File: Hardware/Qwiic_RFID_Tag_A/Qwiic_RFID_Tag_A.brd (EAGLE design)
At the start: 25.4 x 50.8 mm, 46 parts, among them J1 Qwiic, J2 Qwiic, U1 ST25DV64KC

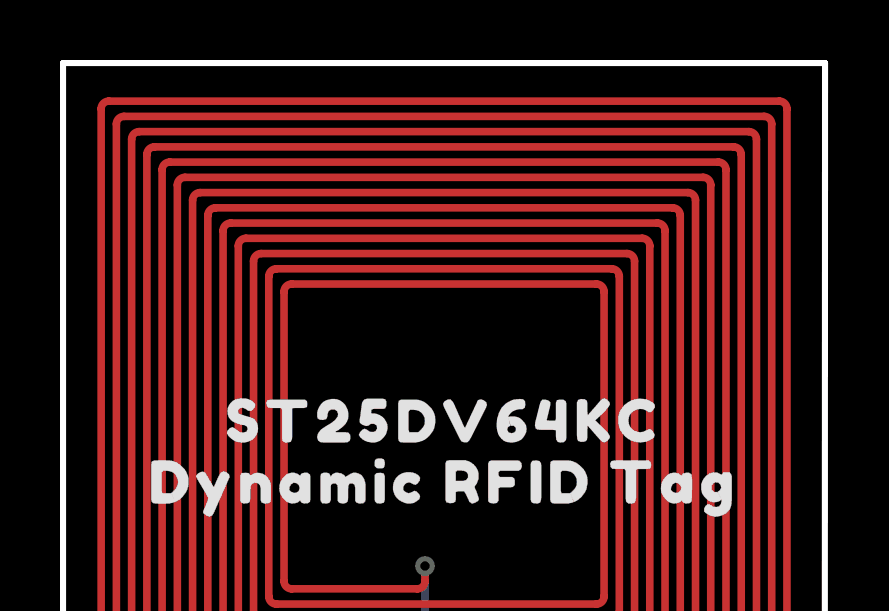
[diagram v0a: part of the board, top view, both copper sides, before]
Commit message: Update aesthetics
Add SFE logo
Update version number
Change schematic frame to correct version
Update design attribution
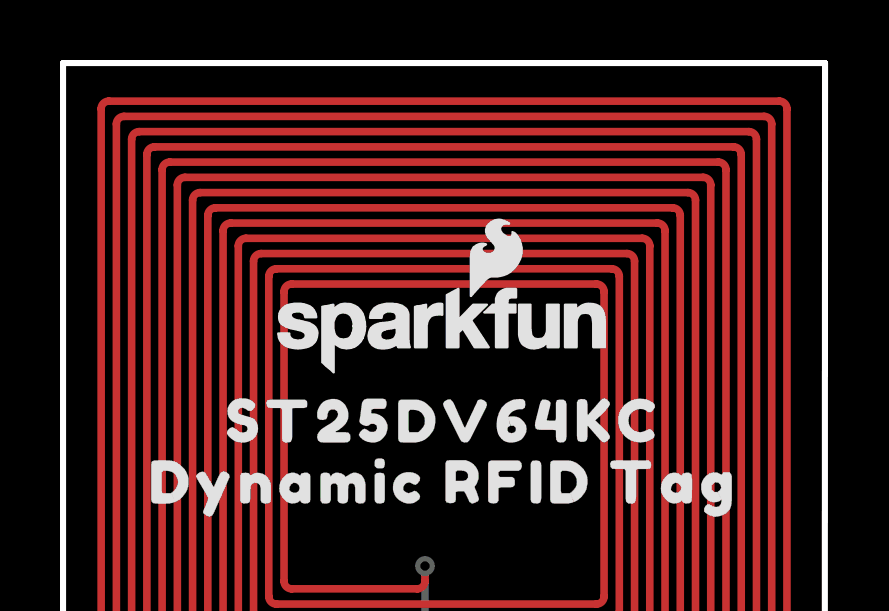
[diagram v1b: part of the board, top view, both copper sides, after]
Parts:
- removed FRAME1: FRAME-LETTERNO_PACKAGE, SparkFun-Aesthetics:DUMMY
- added FRAME2: FRAME-LETTER, SparkFun-Aesthetics:CREATIVE_COMMONS
- added LOGO2, LOGO4: SFE_LOGO_NAME_FLAME.1_INCH, SparkFun-Aesthetics:SFE_LOGO_NAME_FLAME_.1
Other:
- board text added: "Revised by: Dryw Wade"
- board text added: "Ricardo Ramos"
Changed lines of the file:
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@@
 <drawing>
 <settings>
-<setting alwaysvectorfont="no"/>
+<setting alwaysvectorfont="yes"/>
 <setting verticaltext="up"/>
 </settings>
@@
 <layer number="38" name="bTest" color="7" fill="1" visible="no" active="yes"/>
 <layer number="39" name="tKeepout" color="4" fill="11" visible="yes" active="yes"/>
-<layer number="40" name="bKeepout" color="1" fill="11" visible="yes" active="yes"/>
+<layer number="40" name="bKeepout" color="1" fill="11" visible="no" active="yes"/>
 <layer number="41" name="tRestrict" color="4" fill="10" visible="yes" active="yes"/>
-<layer number="42" name="bRestrict" color="1" fill="10" visible="yes" active="yes"/>
-<layer number="43" name="vRestrict" color="2" fill="10" visible="yes" active="yes"/>
+<layer number="42" name="bRestrict" color="1" fill="10" visible="no" active="yes"/>
+<layer number="43" name="vRestrict" color="2" fill="10" visible="no" active="yes"/>
 <layer number="44" name="Drills" color="7" fill="1" visible="no" active="yes"/>
 <layer number="45" name="Holes" color="7" fill="1" visible="yes" active="yes"/>
-<layer number="46" name="Milling" color="3" fill="1" visible="yes" active="yes"/>
+<layer number="46" name="Milling" color="3" fill="1" visible="no" active="yes"/>
 <layer number="47" name="Measures" color="7" fill="1" visible="yes" active="yes"/>
 <layer number="48" name="Document" color="7" fill="1" visible="no" active="yes"/>
@@
 <layer number="50" name="dxf" color="7" fill="1" visible="no" active="no"/>
 <layer number="51" name="tDocu" color="6" fill="1" visible="yes" active="yes"/>
-<layer number="52" name="bDocu" color="7" fill="1" visible="yes" active="yes"/>
+<layer number="52" name="bDocu" color="7" fill="1" visible="no" active="yes"/>
 <layer number="53" name="tGND_GNDA" color="7" fill="9" visible="no" active="no"/>
 <layer number="54" name="bGND_GNDA" color="1" fill="9" visible="no" active="no"/>
@@
 <dimension x1="0" y1="0" x2="0" y2="22.86" x3="-8.89" y3="11.43" textsize="1.778" textratio="15" layer="47" unit="inch"/>
 <dimension x1="0" y1="0" x2="0" y2="50.8" x3="-12.7" y3="25.4" textsize="1.778" textratio="15" layer="47" unit="inch"/>
+<text x="16.51" y="-29.21" size="1.778" layer="51" font="vector">Ricardo Ramos</text>
+<text x="2.54" y="-31.75" size="1.778" layer="51" font="vector">Revised by: Dryw Wade</text>
 </plain>
 <attributes>
@@
 <attribute name="VALUE" x="22.86" y="19.685" size="0.6096" layer="27" font="vector" ratio="20" rot="R180" align="top-center"/>
 </element>
-<element name="FRAME1" library="SparkFun-Aesthetics" package="DUMMY" value="FRAME-LETTERNO_PACKAGE" x="0" y="0" smashed="yes">
-<attribute name="DESIGNER" value="Ricardo Ramos" x="33.02" y="-38.1" size="1.778" layer="27" display="off"/>
-<attribute name="REV" value="X02" x="0" y="0" size="1.778" layer="27" display="off"/>
-<attribute name="VERSION" value="x01" x="33.02" y="-38.1" size="1.778" layer="27" display="off"/>
-</element>
 <element name="J1" library="SparkFun-Connectors" package="JST04_1MM_RA" value="Qwiic" x="20.32" y="12.7" smashed="yes" rot="R90">
 <attribute name="NAME" x="22.479" y="11.303" size="0.6096" layer="25" font="vector" ratio="20" rot="R90"/>
@@
 <element name="U$11" library="output" package="DYNAMIC_RFID_TAG0" value="" x="12.7" y="36.83" smashed="yes" rot="MR0"/>
 <element name="U$1" library="output" package="#I2C#0" value="" x="9.525" y="12.7" smashed="yes" rot="MR0"/>
+<element name="FRAME2" library="SparkFun-Aesthetics" package="CREATIVE_COMMONS" value="FRAME-LETTER" x="-10.16" y="-29.21" smashed="yes">
+<attribute name="DESIGNER" value="" x="-10.16" y="-29.21" size="1.778" layer="27" display="off"/>
+<attribute name="REV" value="" x="-10.16" y="-29.21" size="1.778" layer="27" display="off"/>
+</element>
+<element name="LOGO2" library="SparkFun-Aesthetics" package="SFE_LOGO_NAME_FLAME_.1" value="SFE_LOGO_NAME_FLAME.1_INCH" x="12.7" y="41.91" smashed="yes"/>
+<element name="LOGO4" library="SparkFun-Aesthetics" package="SFE_LOGO_NAME_FLAME_.1" value="SFE_LOGO_NAME_FLAME.1_INCH" x="12.7" y="41.91" smashed="yes" rot="MR0"/>
 </elements>
 <signals>

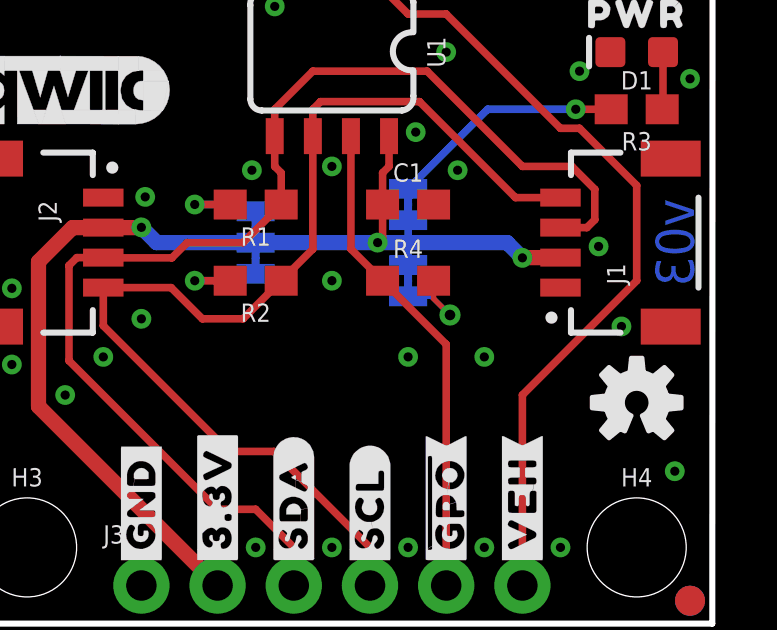
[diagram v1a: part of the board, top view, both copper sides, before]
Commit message: Design review updates
All scehmatics:
Change IC text to “Dynamic RFID Tag - ST25DV64KC”
Move decoupling capacitor near IC
Update I2C jumper text to say "traces" instead of "trace"

Version A board:
Fix stray via diameter
Approve jumper overlap error

Version C board:
Add SFE logo to bottom silk
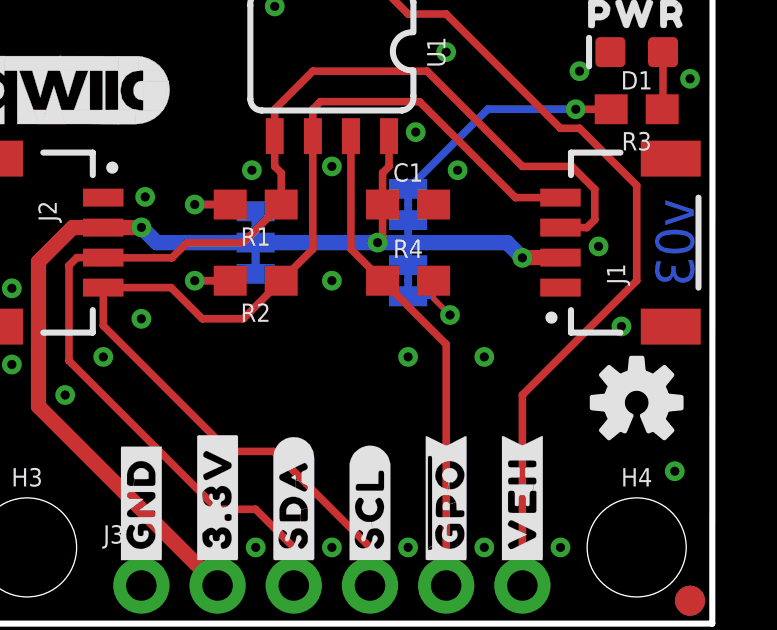
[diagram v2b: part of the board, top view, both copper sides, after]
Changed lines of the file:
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@@
 <drawing>
 <settings>
-<setting alwaysvectorfont="yes"/>
+<setting alwaysvectorfont="no"/>
 <setting verticaltext="up"/>
 </settings>
@@
 <wire x1="16.09" y1="11.43" x2="16.09" y2="10.834" width="0.1778" layer="1"/>
 <wire x1="16.09" y1="10.834" x2="16.637" y2="10.287" width="0.1778" layer="1"/>
-<via x="16.637" y="10.287" extent="1-16" drill="0.35"/>
+<via x="16.637" y="10.287" extent="1-16" drill="0.3048"/>
 <wire x1="16.637" y1="10.287" x2="16.0147" y2="10.9093" width="0.1778" layer="16"/>
 <wire x1="16.0147" y1="10.9093" x2="15.24" y2="10.9093" width="0.1778" layer="16"/>

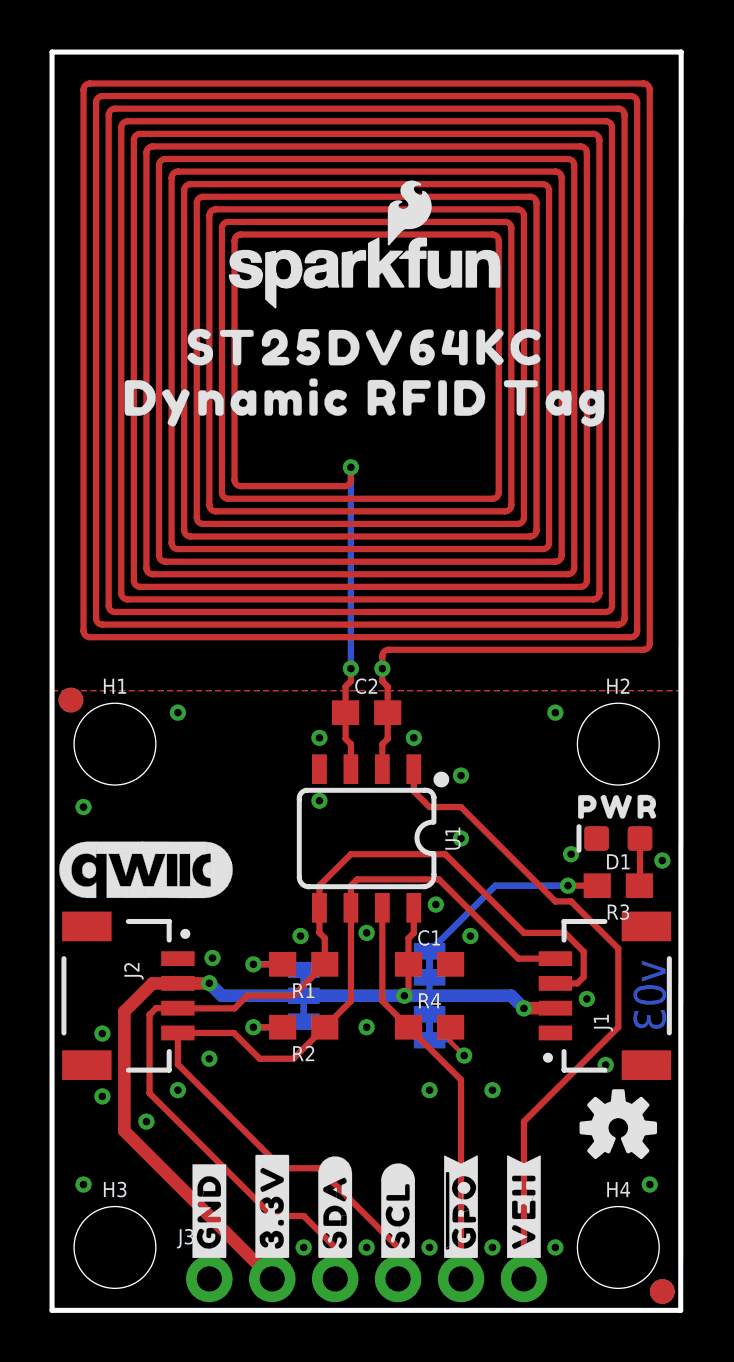
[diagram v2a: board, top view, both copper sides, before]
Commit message: Design review updates
Add version letter to silk
Add I2C addresses to schematic
Change PTH silk labels from "3.3V" to "3V3"
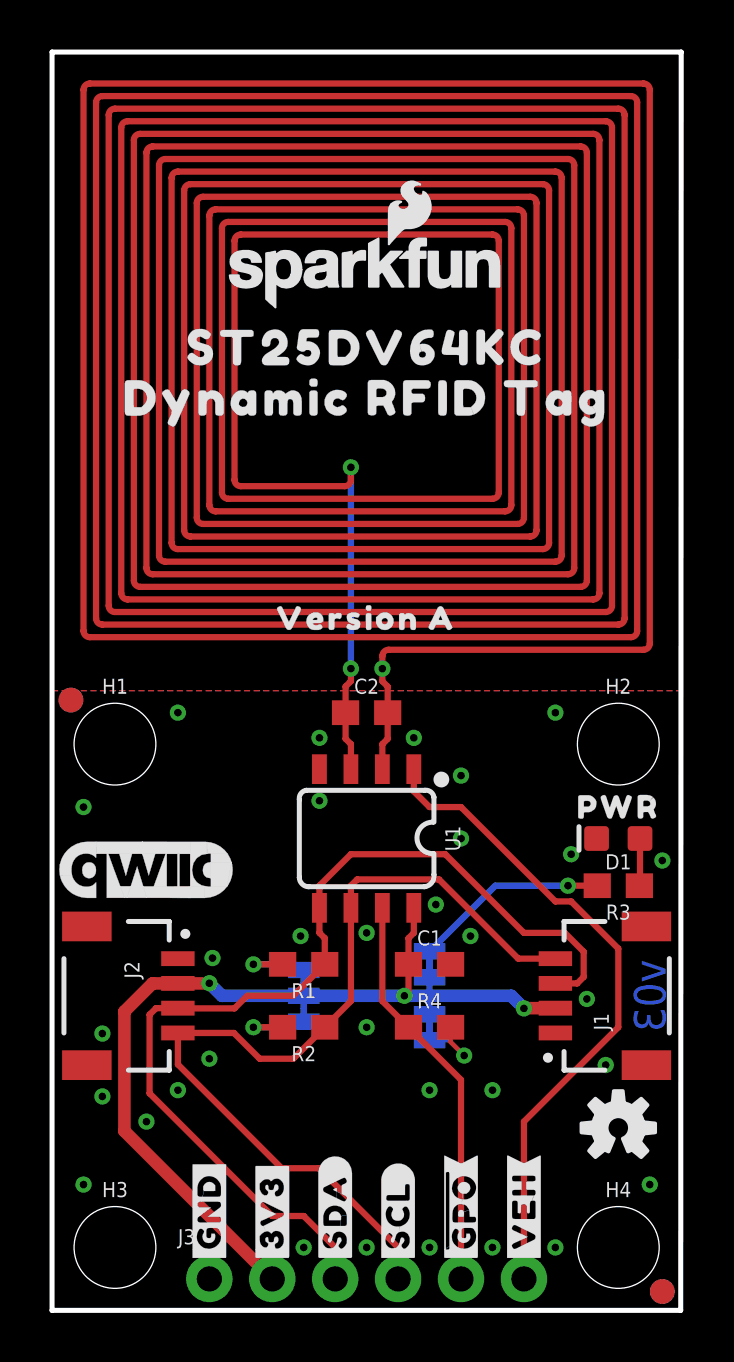
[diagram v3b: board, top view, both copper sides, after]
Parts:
- removed U$19: (no value), output:#3#3V#0
- added U$12: (no value), output:VERSION_A0
- added U$2: (no value), output:#3V3#0
- U$3: device output:#3#3V#0 -> output:#3V3#0
- flipped U$3 to the bottom
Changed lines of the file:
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@@
 <drawing>
 <settings>
-<setting alwaysvectorfont="no"/>
+<setting alwaysvectorfont="yes"/>
 <setting verticaltext="up"/>
 </settings>
@@
 <layer number="38" name="bTest" color="7" fill="1" visible="no" active="yes"/>
 <layer number="39" name="tKeepout" color="4" fill="11" visible="yes" active="yes"/>
-<layer number="40" name="bKeepout" color="1" fill="11" visible="no" active="yes"/>
+<layer number="40" name="bKeepout" color="1" fill="11" visible="yes" active="yes"/>
 <layer number="41" name="tRestrict" color="4" fill="10" visible="yes" active="yes"/>
-<layer number="42" name="bRestrict" color="1" fill="10" visible="no" active="yes"/>
-<layer number="43" name="vRestrict" color="2" fill="10" visible="no" active="yes"/>
+<layer number="42" name="bRestrict" color="1" fill="10" visible="yes" active="yes"/>
+<layer number="43" name="vRestrict" color="2" fill="10" visible="yes" active="yes"/>
 <layer number="44" name="Drills" color="7" fill="1" visible="no" active="yes"/>
 <layer number="45" name="Holes" color="7" fill="1" visible="yes" active="yes"/>
-<layer number="46" name="Milling" color="3" fill="1" visible="no" active="yes"/>
+<layer number="46" name="Milling" color="3" fill="1" visible="yes" active="yes"/>
 <layer number="47" name="Measures" color="7" fill="1" visible="yes" active="yes"/>
 <layer number="48" name="Document" color="7" fill="1" visible="no" active="yes"/>
@@
 <layer number="50" name="dxf" color="7" fill="1" visible="no" active="no"/>
 <layer number="51" name="tDocu" color="6" fill="1" visible="yes" active="yes"/>
-<layer number="52" name="bDocu" color="7" fill="1" visible="no" active="yes"/>
+<layer number="52" name="bDocu" color="7" fill="1" visible="yes" active="yes"/>
 <layer number="53" name="tGND_GNDA" color="7" fill="9" visible="no" active="no"/>
 <layer number="54" name="bGND_GNDA" color="1" fill="9" visible="no" active="no"/>
@@
 <attribute name="VALUE" x="22.86" y="0.508" size="0.6096" layer="27" font="vector" ratio="20" align="top-center"/>
 </element>
-<element name="U$3" library="output" package="#3#3V#0" value="" x="8.89" y="1.778" smashed="yes" rot="R90"/>
 <element name="U$4" library="output" package="#GND#4" value="" x="6.35" y="1.778" smashed="yes" rot="R90"/>
 <element name="U$5" library="output" package="#SDA#5" value="" x="11.43" y="1.778" smashed="yes" rot="R90"/>
@@
 <element name="U$17" library="output" package="#LED#10" value="" x="15.875" y="13.97" smashed="yes" rot="MR0"/>
 <element name="U$18" library="output" package="#GND#4" value="" x="6.35" y="1.778" smashed="yes" rot="MR90"/>
-<element name="U$19" library="output" package="#3#3V#0" value="" x="8.89" y="1.778" smashed="yes" rot="MR90"/>
 <element name="U$20" library="output" package="#SDA#5" value="" x="11.43" y="1.778" smashed="yes" rot="MR90"/>
 <element name="U$21" library="output" package="#SCL#6" value="" x="13.97" y="1.778" smashed="yes" rot="MR90"/>
@@
 <element name="LOGO2" library="SparkFun-Aesthetics" package="SFE_LOGO_NAME_FLAME_.1" value="SFE_LOGO_NAME_FLAME.1_INCH" x="12.7" y="41.91" smashed="yes"/>
 <element name="LOGO4" library="SparkFun-Aesthetics" package="SFE_LOGO_NAME_FLAME_.1" value="SFE_LOGO_NAME_FLAME.1_INCH" x="12.7" y="41.91" smashed="yes" rot="MR0"/>
+<element name="U$2" library="output" package="#3V3#0" value="" x="8.89" y="1.778" smashed="yes" rot="R90"/>
+<element name="U$3" library="output" package="#3V3#0" value="" x="8.89" y="1.778" smashed="yes" rot="MR90"/>
+<element name="U$12" library="output" package="VERSION_A0" value="" x="12.7" y="27.94" smashed="yes"/>
 </elements>
 <signals>
